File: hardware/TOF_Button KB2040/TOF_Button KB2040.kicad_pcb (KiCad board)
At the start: 2 copper layers, 55.9 x 45.7 mm, 13 parts

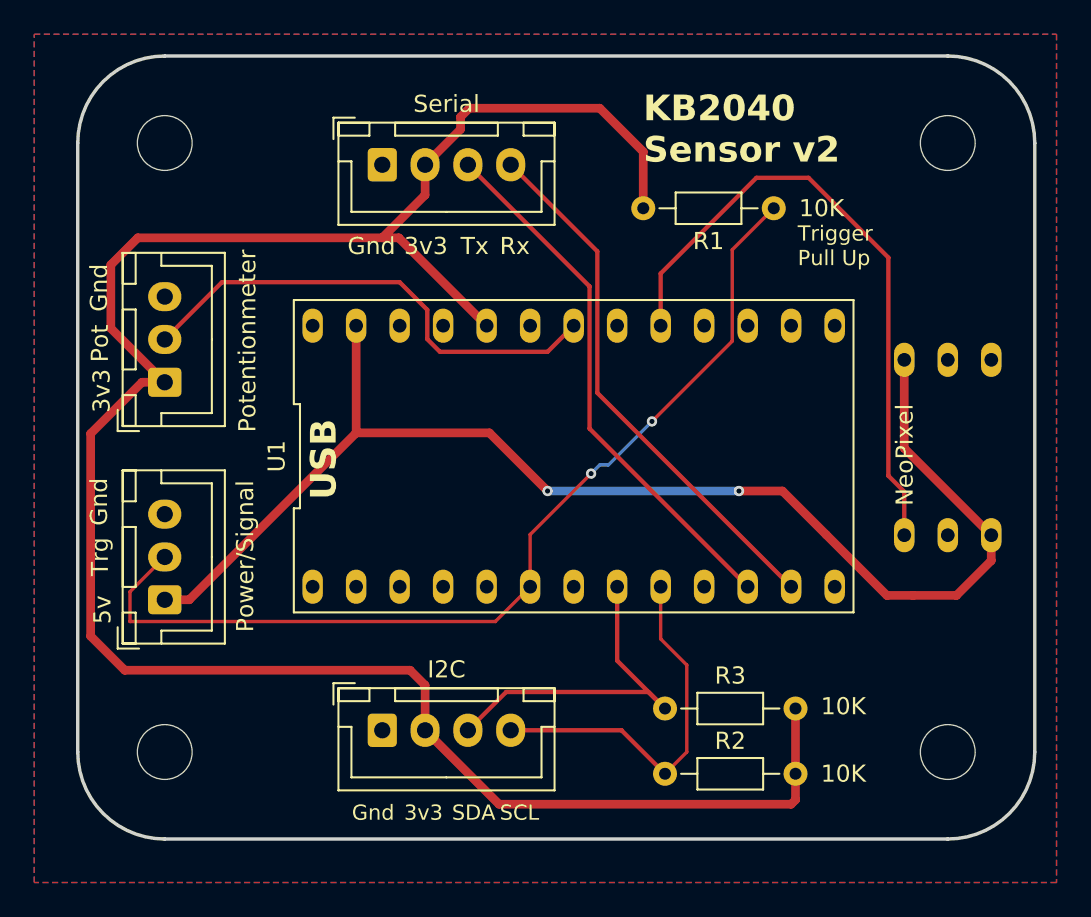
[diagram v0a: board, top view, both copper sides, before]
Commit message: PCB fix for TOF buttons
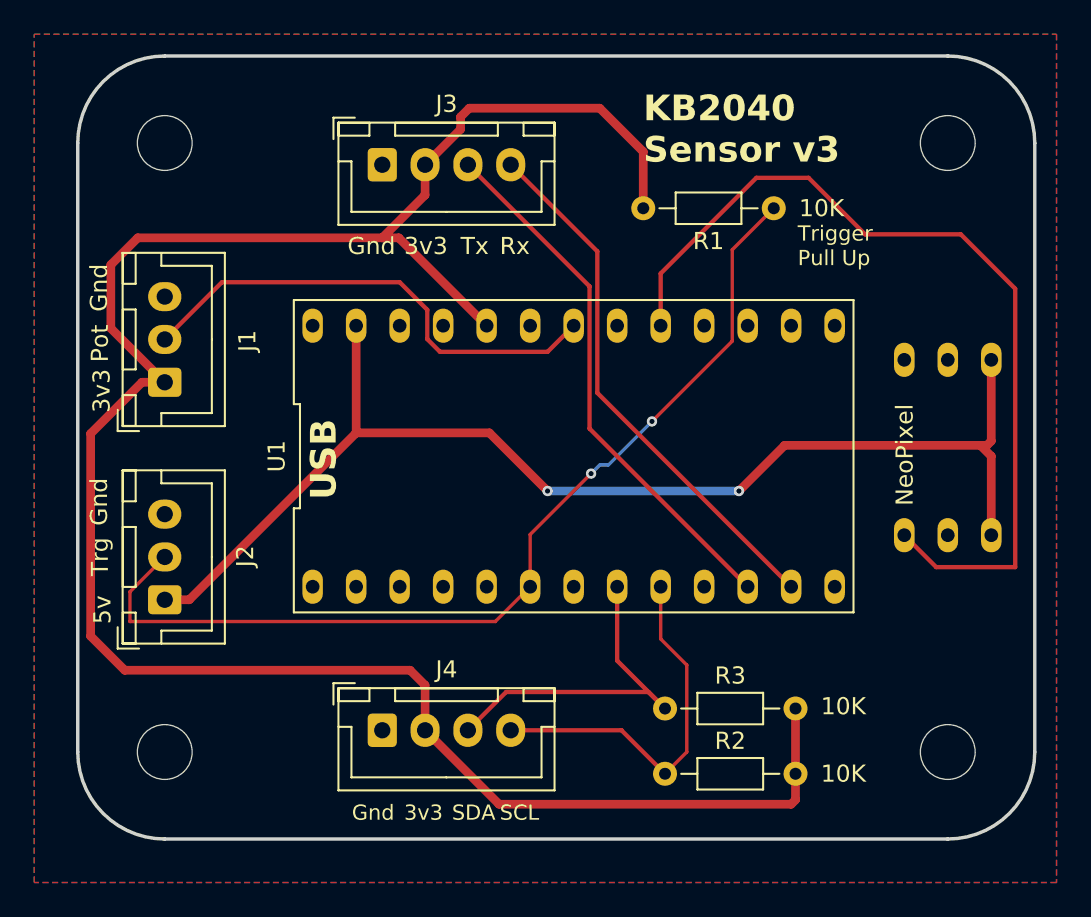
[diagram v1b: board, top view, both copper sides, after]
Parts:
- renumbered Potentionmeter to J1, Power/Signal to J2, Serial to J3, I2C to J4
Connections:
- U2 pad 4: +5V -> unconnected-(U2-DataOut-Pad4)
- U2 pad 6: unconnected-(U2-DataOut-Pad6) -> +5V
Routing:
- net NeoPixel_Data: track 37.2 -> 52.3 mm
- net +5V: track 77.2 -> 71.4 mm
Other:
- board text added: "KB2040 Sensor v3"
- board text removed: "KB2040 Sensor v2"
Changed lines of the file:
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@@
 	(net 9 "SDA")
 	(net 10 "NeoPixel_Data")
-	(net 11 "unconnected-(U2-DataOut-Pad6)")
+	(net 11 "unconnected-(U2-DataOut-Pad4)")
 	(net 12 "unconnected-(U1-D--Pad26)")
 	(net 13 "unconnected-(U1-MOSI-Pad15)")
@@
 		(descr "JST XH series connector, B3B-XH-A (http://www.jst-mfg.com/product/pdf/eng/eXH.pdf), generated with kicad-footprint-generator")
 		(tags "connector JST XH vertical")
-		(property "Reference" "Power/Signal"
+		(property "Reference" "J2"
 			(at 2.54 4.699 -90)
 			(layer "F.SilkS")
@@
 		(descr "JST XH series connector, B4B-XH-A (http://www.jst-mfg.com/product/pdf/eng/eXH.pdf), generated with kicad-footprint-generator")
 		(tags "connector JST XH vertical")
-		(property "Reference" "I2C"
+		(property "Reference" "J4"
 			(at 3.75 -3.55 0)
 			(layer "F.SilkS")
@@
 		(descr "JST XH series connector, B4B-XH-A (http://www.jst-mfg.com/product/pdf/eng/eXH.pdf), generated with kicad-footprint-generator")
 		(tags "connector JST XH vertical")
-		(property "Reference" "Serial"
+		(property "Reference" "J3"
 			(at 3.75 -3.55 0)
 			(layer "F.SilkS")
@@
 		(descr "JST XH series connector, B3B-XH-A (http://www.jst-mfg.com/product/pdf/eng/eXH.pdf), generated with kicad-footprint-generator")
 		(tags "connector JST XH vertical")
-		(property "Reference" "Potentionmeter"
+		(property "Reference" "J1"
 			(at 2.413 4.826 -90)
 			(layer "F.SilkS")
@@
 			(layers "*.Cu" "*.Mask")
 			(remove_unused_layers no)
-			(net 4 "+5V")
-			(pinfunction "5v")
-			(pintype "input")
+			(net 11 "unconnected-(U2-DataOut-Pad4)")
+			(pinfunction "DataOut")
+			(pintype "output+no_connect")
 			(thermal_bridge_angle 45)
 		)
@@
 			(layers "*.Cu" "*.Mask")
 			(remove_unused_layers no)
-			(net 11 "unconnected-(U2-DataOut-Pad6)")
-			(pinfunction "DataOut")
-			(pintype "output+no_connect")
+			(net 4 "+5V")
+			(pinfunction "5v")
+			(pintype "input")
 			(thermal_bridge_angle 45)
 		)
@@
 	)
 	(gr_text "5v"
-		(at 182.245 87.122 -90)
+		(at 187.325 87.249 -90)
 		(layer "B.SilkS")
 		(effects
@@
 	)
 	(gr_text "NC"
-		(at 187.325 87.249 270)
+		(at 182.245 87.249 270)
 		(layer "B.SilkS")
 		(effects
@@
 		)
 	)
-	(gr_text "KB2040\nSensor v2"
+	(gr_text "KB2040\nSensor v3"
 		(at 167.64 77.47 0)
 		(layer "F.SilkS")
@@
 	)
 	(segment
-		(start 150.876 93.126)
-		(end 150.876 86.868)
-		(width 0.508)
-		(layer "F.Cu")
-		(net 4)
-	)
-	(segment
 		(start 187.96 99.1)
-		(end 187.96 100.584)
+		(end 187.96 94.488)
 		(width 0.508)
 		(layer "F.Cu")
@@
 	)
 	(segment
-		(start 178.308 99.06)
-		(end 175.768 96.52)
+		(start 173.228 96.52)
+		(end 175.895 93.853)
 		(width 0.508)
 		(layer "F.Cu")
@@
 	)
 	(segment
-		(start 182.88 94.02)
-		(end 187.96 99.1)
+		(start 150.876 93.126)
+		(end 150.876 86.868)
 		(width 0.508)
 		(layer "F.Cu")
@@
 	)
 	(segment
-		(start 182.88 88.86)
-		(end 182.88 94.02)
+		(start 187.706 93.853)
+		(end 187.96 93.599)
 		(width 0.508)
 		(layer "F.Cu")
@@
 	)
 	(segment
-		(start 150.876 93.126)
-		(end 158.658 93.126)
+		(start 187.325 93.853)
+		(end 187.706 93.853)
 		(width 0.508)
 		(layer "F.Cu")
@@
 	)
 	(segment
-		(start 175.768 96.52)
-		(end 173.228 96.52)
+		(start 175.895 93.853)
+		(end 187.325 93.853)
 		(width 0.508)
 		(layer "F.Cu")
@@
 	)
 	(segment
-		(start 183.388 102.616)
-		(end 181.864 102.616)
+		(start 150.876 93.126)
+		(end 158.658 93.126)
 		(width 0.508)
 		(layer "F.Cu")
@@
 	)
 	(segment
-		(start 185.928 102.616)
-		(end 183.388 102.616)
+		(start 187.96 94.488)
+		(end 187.325 93.853)
 		(width 0.508)
 		(layer "F.Cu")
@@
 	)
 	(segment
-		(start 181.864 102.616)
-		(end 178.308 99.06)
-		(width 0.508)
-		(layer "F.Cu")
-		(net 4)
-	)
-	(segment
-		(start 187.96 100.584)
-		(end 185.928 102.616)
+		(start 141.132 102.87)
+		(end 150.876 93.126)
 		(width 0.508)
 		(layer "F.Cu")
@@
 	)
 	(segment
-		(start 141.132 102.87)
-		(end 150.876 93.126)
+		(start 187.96 93.599)
+		(end 187.96 88.86)
 		(width 0.508)
 		(layer "F.Cu")
@@
 	)
 	(segment
+		(start 182.88 99.1)
+		(end 184.745 100.965)
+		(width 0.254)
+		(layer "F.Cu")
+		(net 10)
+	)
+	(segment
+		(start 189.357 84.709)
+		(end 186.182 81.534)
+		(width 0.254)
+		(layer "F.Cu")
+		(net 10)
+	)
+	(segment
 		(start 174.244 78.232)
 		(end 168.656 83.82)
@@
 	)
 	(segment
-		(start 168.656 83.82)
-		(end 168.656 86.868)
+		(start 180.594 81.534)
+		(end 177.292 78.232)
 		(width 0.254)
 		(layer "F.Cu")
@@
 	)
 	(segment
-		(start 182.88 99.1)
-		(end 182.88 96.56)
+		(start 186.182 81.534)
+		(end 180.594 81.534)
 		(width 0.254)
 		(layer "F.Cu")
@@
 	)
 	(segment
-		(start 181.953 95.633)
-		(end 181.953 82.893)
+		(start 177.292 78.232)
+		(end 174.244 78.232)
 		(width 0.254)
 		(layer "F.Cu")
@@
 	)
 	(segment
-		(start 181.953 82.893)
-		(end 177.292 78.232)
+		(start 184.745 100.965)
+		(end 189.357 100.965)
 		(width 0.254)
 		(layer "F.Cu")
@@
 	)
 	(segment
-		(start 182.88 96.56)
-		(end 181.953 95.633)
+		(start 189.357 100.965)
+		(end 189.357 84.709)
 		(width 0.254)
 		(layer "F.Cu")
@@
 	)
 	(segment
-		(start 177.292 78.232)
-		(end 174.244 78.232)
+		(start 168.656 83.82)
+		(end 168.656 86.868)
 		(width 0.254)
 		(layer "F.Cu")
